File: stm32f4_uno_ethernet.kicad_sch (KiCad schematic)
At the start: 11 parts, among them J101 STM32 GPIO, J102 Digital/PWM, J103 STM32 GPIO, J104 STM32 GPIO, J105 STM32 GPIO, J106 Power, J107 Ethernet, J108 STM32 GPIO, J109 Digital/PWM, J110 Analog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

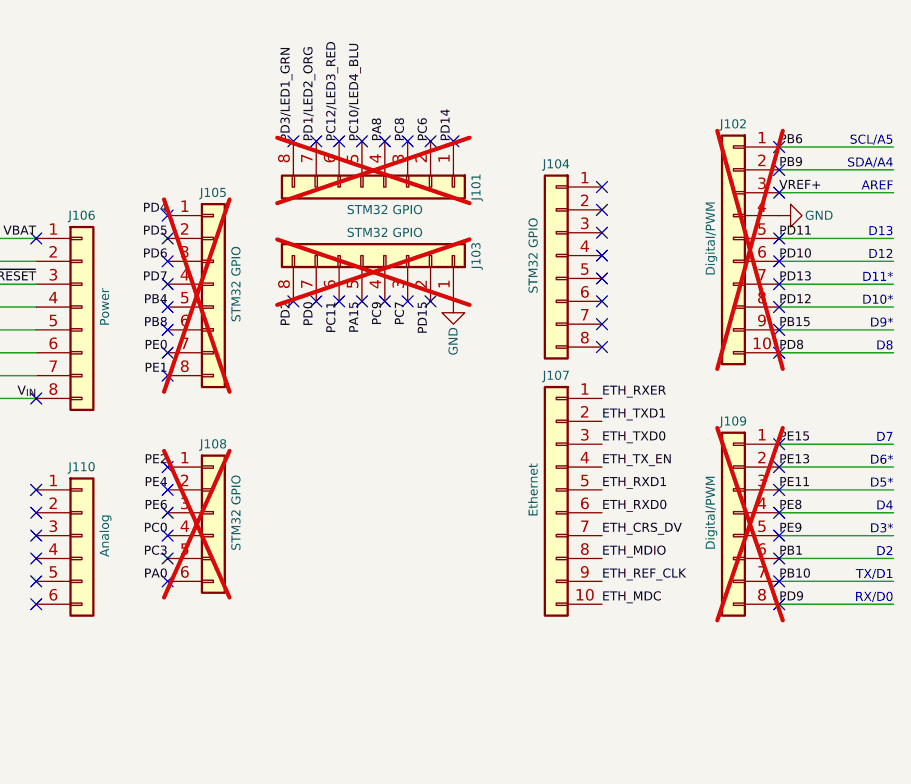
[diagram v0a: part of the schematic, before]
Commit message: #8 Add all pin sockets on ethernet
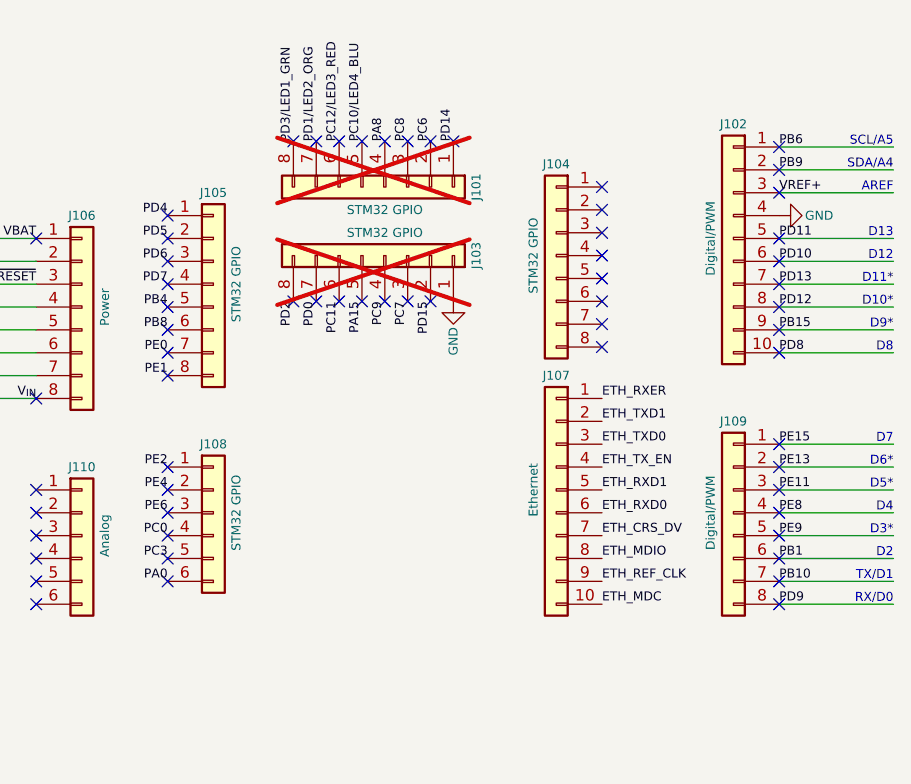
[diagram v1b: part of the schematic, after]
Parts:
- J102, J105, J108, J109: now fitted
